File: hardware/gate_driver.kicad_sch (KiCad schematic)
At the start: 9 parts, among them U5 DRV8353SRTAR

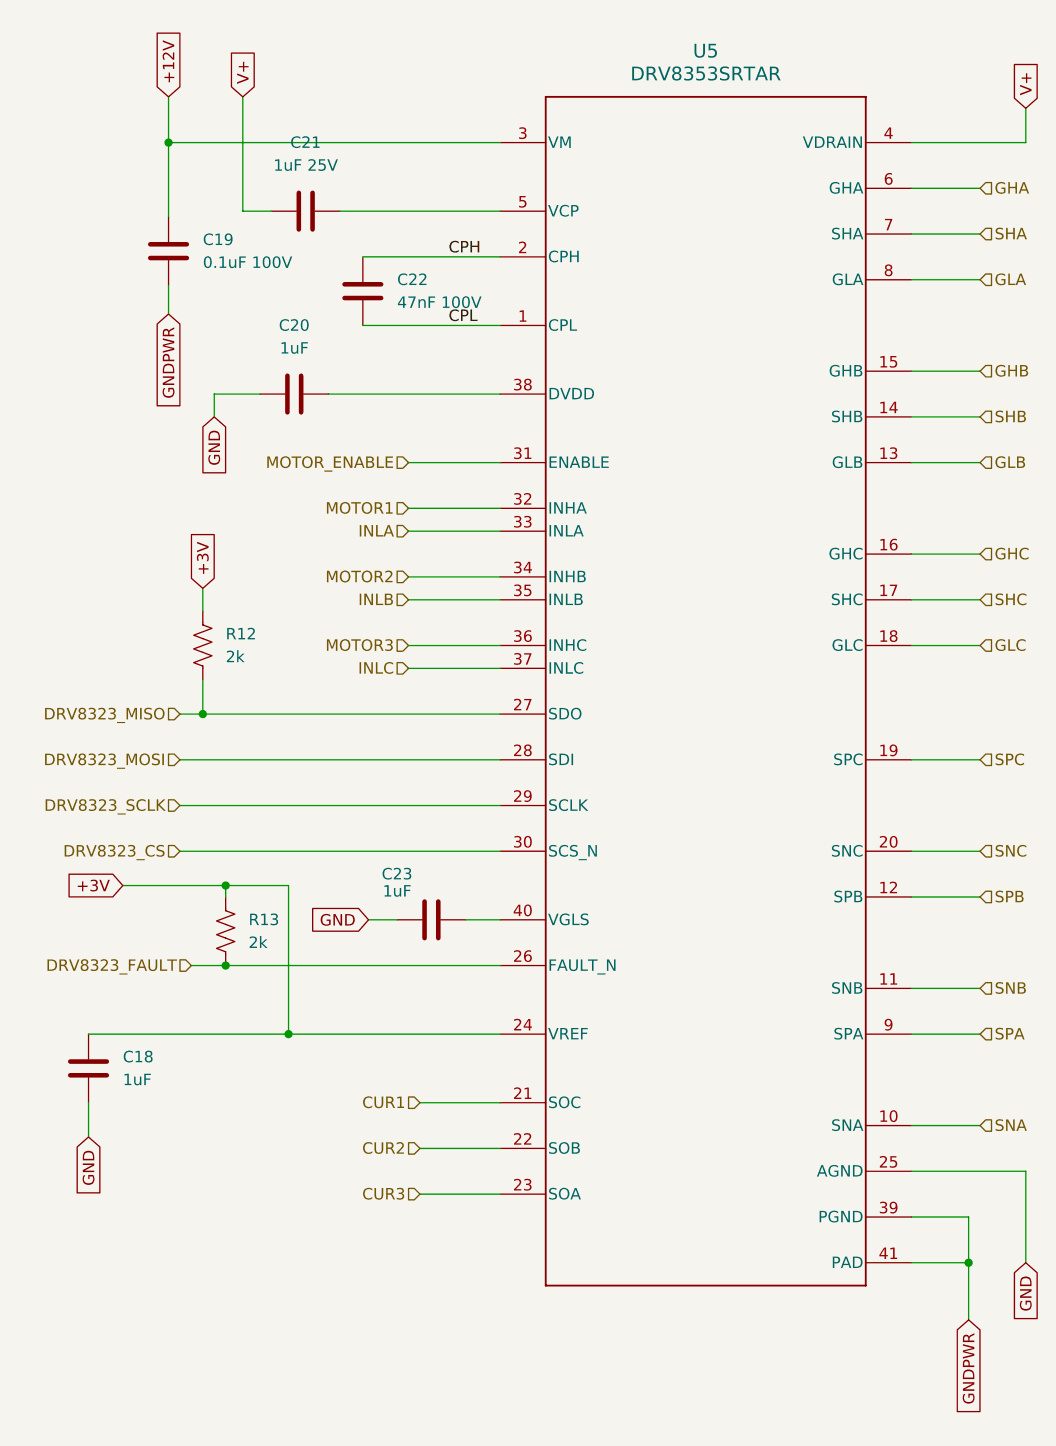
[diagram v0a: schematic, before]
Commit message: Clean up schematic ERC; add project symbol library; update README
Fix dangling labels, floating pins and pin types across the sheets so
ERC reports 0 errors (see hardware/CHANGES.txt). Add PWR_FLAGs and move
TCAN1042GV, MA702GQ and the EMI filter to nexus_drive.kicad_sym.

Update the README layout, specs and schematic review status.

Co-Authored-By: Claude Opus 5.5 <noreply@anthropic.com>
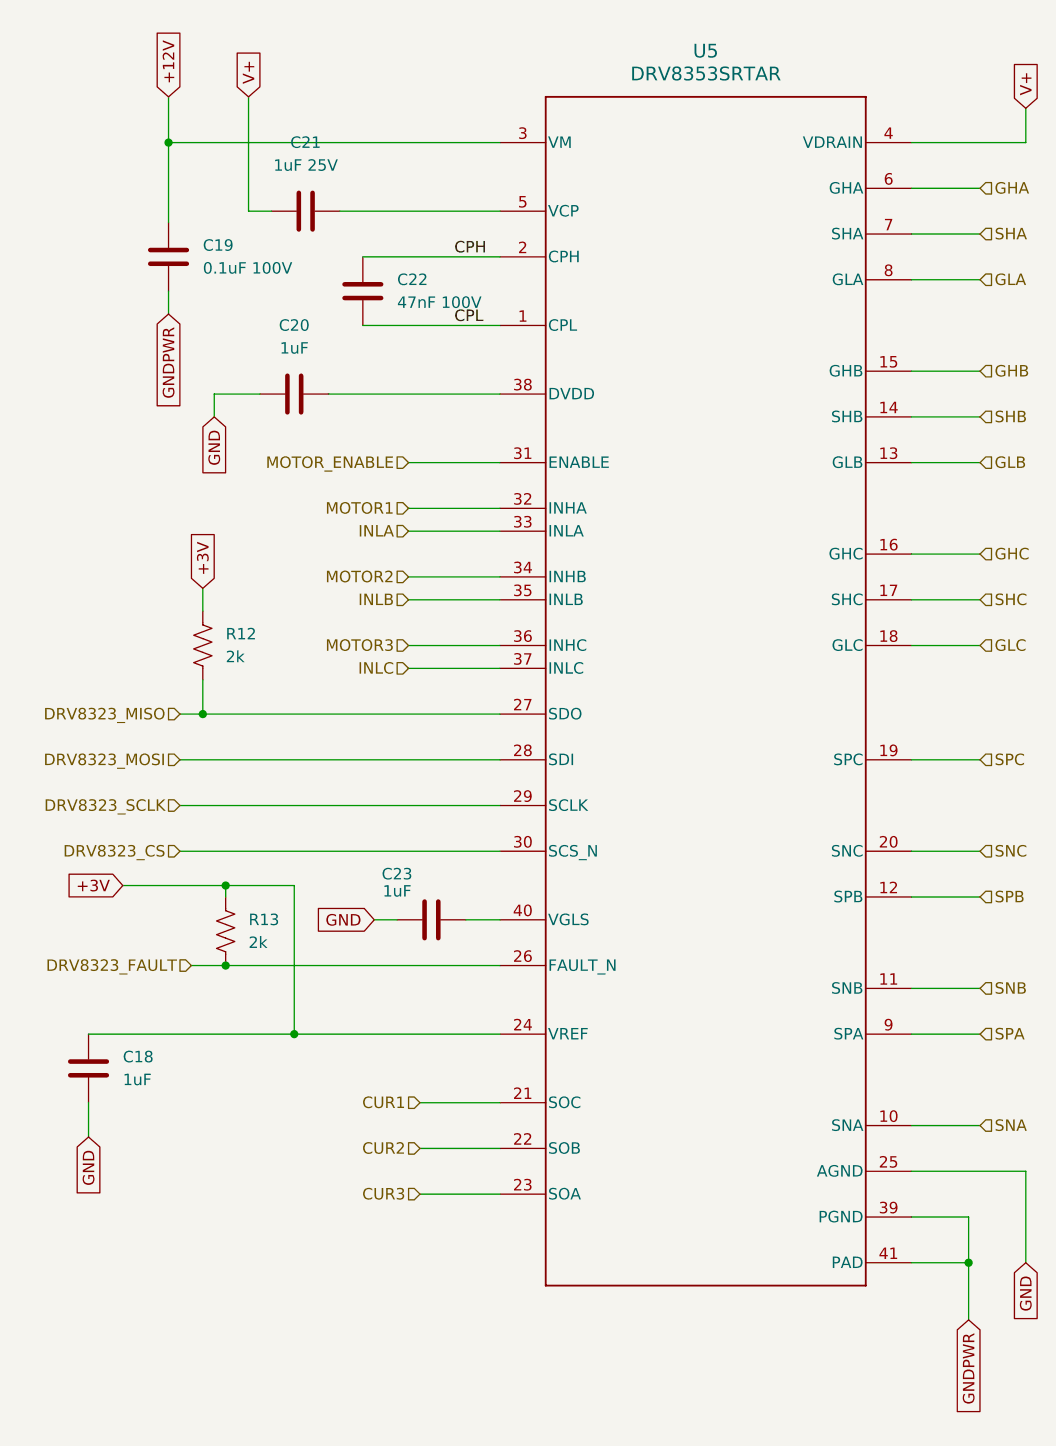
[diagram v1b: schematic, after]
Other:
- moved on the sheet: C19
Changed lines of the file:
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@@
 	)
 	(junction
-		(at 60.325 133.35)
+		(at 60.96 133.35)
 		(diameter 0)
 		(color 0 0 0 0)
@@
 	(wire
 		(pts
-			(xy 60.325 133.35) (xy 83.82 133.35)
+			(xy 60.96 133.35) (xy 83.82 133.35)
 		)
 		(stroke
@@
 	(wire
 		(pts
-			(xy 55.245 29.21) (xy 55.245 41.91)
+			(xy 55.88 29.21) (xy 55.88 41.91)
 		)
 		(stroke
@@
 	(wire
 		(pts
-			(xy 55.245 41.91) (xy 58.42 41.91)
+			(xy 55.88 41.91) (xy 58.42 41.91)
 		)
 		(stroke
@@
 	(wire
 		(pts
-			(xy 69.215 120.65) (xy 72.39 120.65)
+			(xy 69.85 120.65) (xy 72.39 120.65)
 		)
 		(stroke
@@
 	(wire
 		(pts
-			(xy 46.99 34.29) (xy 46.99 42.545)
+			(xy 46.99 34.29) (xy 46.99 43.18)
 		)
 		(stroke
@@
 	(wire
 		(pts
-			(xy 53.34 116.84) (xy 60.325 116.84)
+			(xy 53.34 116.84) (xy 60.96 116.84)
 		)
 		(stroke
@@
 	(wire
 		(pts
-			(xy 60.325 116.84) (xy 60.325 133.35)
+			(xy 60.96 116.84) (xy 60.96 133.35)
 		)
 		(stroke
@@
 	(wire
 		(pts
-			(xy 46.99 50.165) (xy 46.99 53.34)
+			(xy 46.99 50.8) (xy 46.99 53.34)
 		)
 		(stroke
@@
 	(wire
 		(pts
-			(xy 38.1 133.35) (xy 60.325 133.35)
+			(xy 38.1 133.35) (xy 60.96 133.35)
 		)
 		(stroke
@@
 	)
 	(label "CPL"
-		(at 78.105 54.61 0)
+		(at 78.74 54.61 0)
 		(effects
 			(font
@@
 	)
 	(label "CPH"
-		(at 78.105 46.99 0)
+		(at 78.74 46.99 0)
 		(effects
 			(font
@@
 	(global_label "GND"
 		(shape input)
-		(at 69.215 120.65 180)
+		(at 69.85 120.65 180)
 		(fields_autoplaced yes)
 		(effects
@@
 		)
 		(property "Intersheetrefs" "${INTERSHEET_REFS}"
-			(at 62.3593 120.65 0)
+			(at 62.9943 120.65 0)
 			(hide yes)
 			(show_name no)
@@
 	(global_label "V+"
 		(shape input)
-		(at 55.245 29.21 90)
+		(at 55.88 29.21 90)
 		(fields_autoplaced yes)
 		(effects
@@
 		)
 		(property "Intersheetrefs" "${INTERSHEET_REFS}"
-			(at 55.245 23.5638 90)
+			(at 55.88 23.5638 90)
 			(hide yes)
 			(show_name no)
@@
 	(symbol
 		(lib_id "Device:C")
-		(at 46.99 46.355 180)
+		(at 46.99 46.99 180)
 		(unit 1)
 		(body_style 1)
@@
 		(fields_autoplaced yes)
 		(property "Reference" "C19"
-			(at 50.8 45.085 0)
+			(at 50.8 45.72 0)
 			(show_name no)
 			(do_not_autoplace no)
@@
 		)
 		(property "Value" "0.1uF 100V"
-			(at 50.8 47.625 0)
+			(at 50.8 48.26 0)
 			(show_name no)
 			(do_not_autoplace no)
@@
 		)
 		(property "Footprint" "Capacitor_SMD:C_0603_1608Metric"
-			(at 46.0248 42.545 0)
+			(at 46.0248 43.18 0)
 			(hide yes)
 			(show_name no)
@@
 		)
 		(property "Datasheet" ""
-			(at 46.99 46.355 0)
-			(hide yes)
-			(show_name no)
-			(do_not_autoplace no)
-			(effects
-				(font
-					(size 1.27 1.27)
-				)
-			)
-		)
-		(property "Description" ""
-			(at 46.99 46.355 0)
+			(at 46.99 46.99 0)
+			(hide yes)
+			(show_name no)
+			(do_not_autoplace no)
+			(effects
+				(font
+					(size 1.27 1.27)
+				)
+			)
+		)
+		(property "Description" "Unpolarized capacitor"
+			(at 46.99 46.99 0)
 			(hide yes)
 			(show_name no)
@@
 		)
 		(property "MPN" "GCJ188R72A104KA01D"
-			(at 46.99 46.355 0)
+			(at 46.99 46.99 0)
 			(hide yes)
 			(show_name no)
@@
 		)
 		(property "MF" "MURATA"
-			(at 46.99 46.355 0)
+			(at 46.99 46.99 0)
 			(hide yes)
 			(show_name no)
@@
 		)
 		(property "POPULATE" "1"
-			(at 46.99 46.355 0)
+			(at 46.99 46.99 0)
 			(hide yes)
 			(show_name no)
@@
 			)
 		)
-		(property "Description" ""
+		(property "Description" "Resistor, US symbol"
 			(at 53.34 121.92 0)
 			(hide yes)
@@
 			)
 		)
-		(property "Description" ""
+		(property "Description" "Unpolarized capacitor"
 			(at 68.58 50.8 0)
 			(hide yes)
@@
 			)
 		)
-		(property "Description" ""
+		(property "Description" "Unpolarized capacitor"
 			(at 38.1 137.16 0)
 			(hide yes)
@@
 			)
 		)
-		(property "Description" ""
+		(property "Description" "Resistor, US symbol"
 			(at 50.8 90.17 0)
 			(hide yes)
@@
 			)
 		)
-		(property "Description" ""
+		(property "Description" "Unpolarized capacitor"
 			(at 76.2 120.65 0)
 			(hide yes)
@@
 			)
 		)
-		(property "Description" ""
+		(property "Description" "Unpolarized capacitor"
 			(at 60.96 62.23 0)
 			(hide yes)
@@
 			)
 		)
-		(property "Description" ""
+		(property "Description" "Unpolarized capacitor"
 			(at 62.23 41.91 0)
 			(hide yes)
